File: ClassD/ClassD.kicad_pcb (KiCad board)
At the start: 2 copper layers, 70.2 x 45.3 mm, 39 parts, among them J1 RCJ-01X, J2 RCJ-01X, P1 CONN_01X02, SW1 FSM2JSMAA, U1 AP1117E50G-13, U2 TPA2008D2

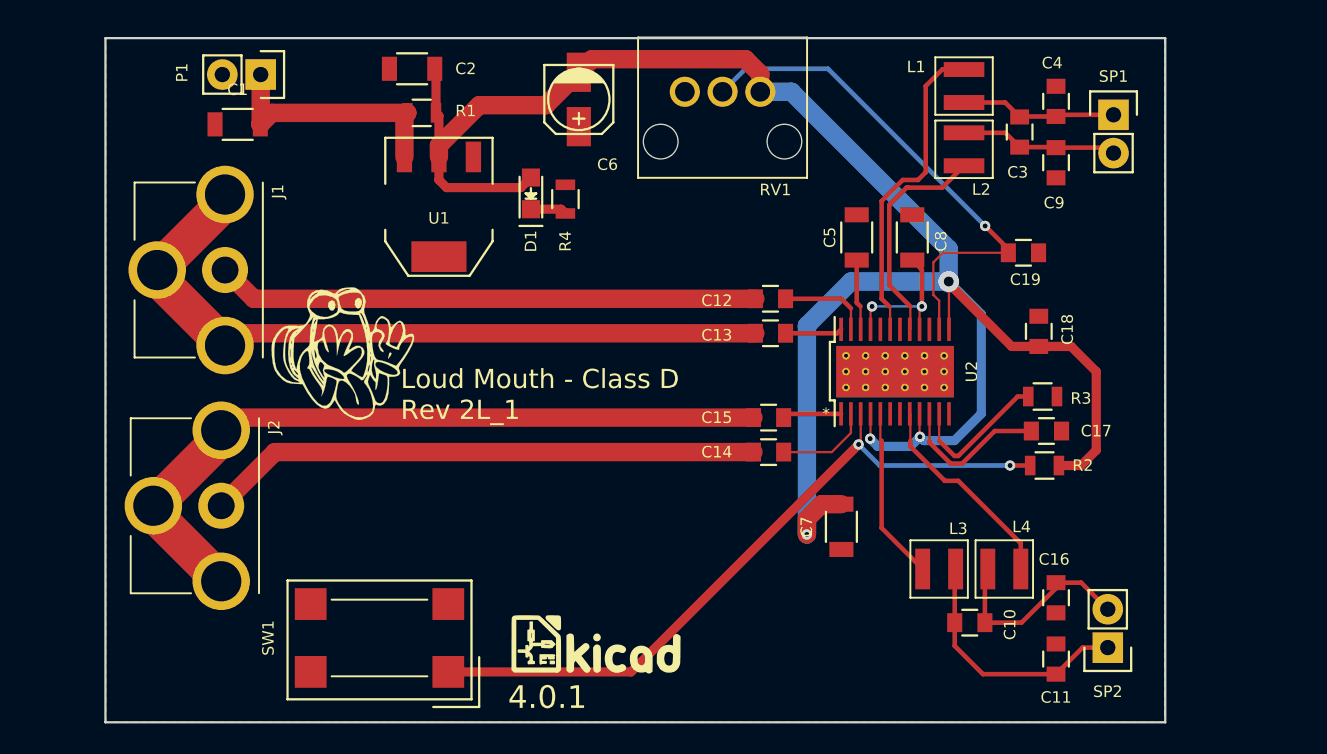
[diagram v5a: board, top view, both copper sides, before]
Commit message: Stitched the ground planes
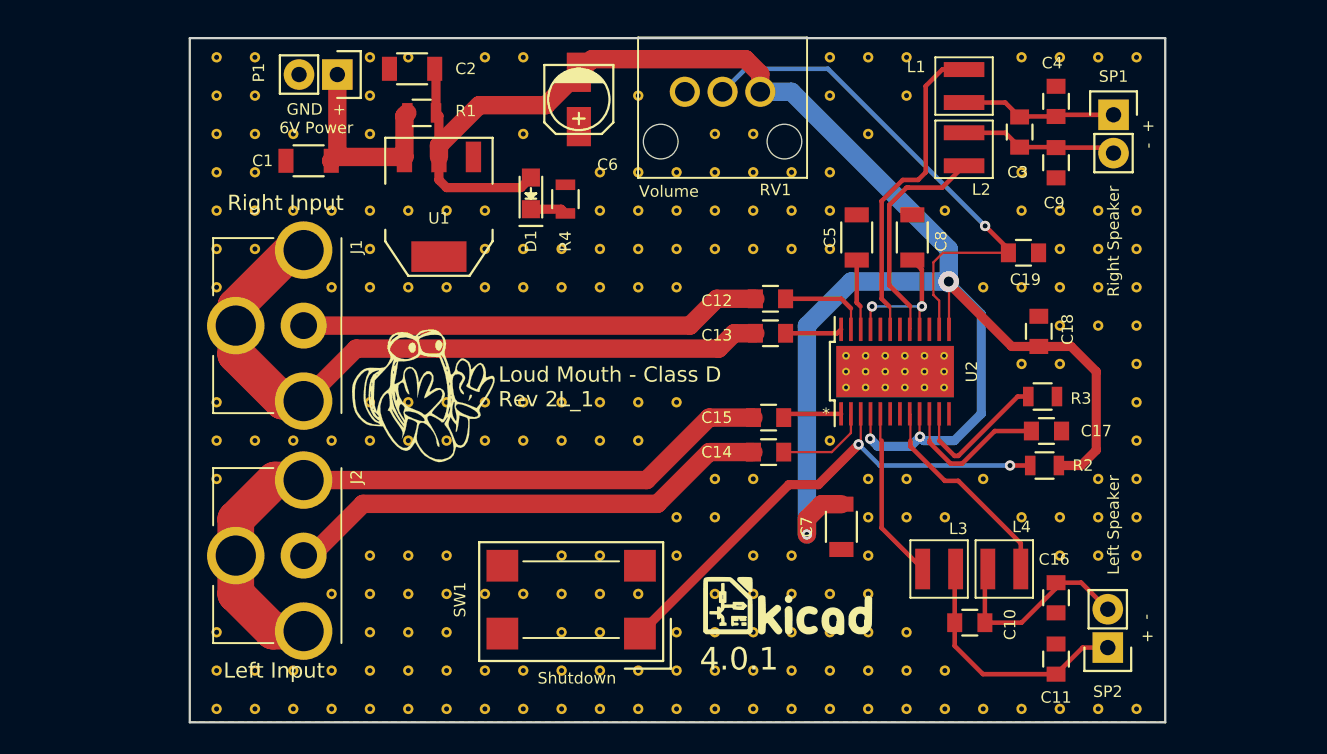
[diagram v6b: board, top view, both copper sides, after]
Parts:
- added ST**111111010: Stitch_VIA, LoudMouth-ClassD:Stitch_VIA, F.Cu at (123.2, 106.7)
- added ST**111111011: Stitch_VIA, LoudMouth-ClassD:Stitch_VIA, F.Cu at (123.2, 109.2)
- added ST**111111014: Stitch_VIA, LoudMouth-ClassD:Stitch_VIA, F.Cu at (123.2, 116.8)
- added ST**111111015: Stitch_VIA, LoudMouth-ClassD:Stitch_VIA, F.Cu at (123.2, 119.4)
- added ST**111111016: Stitch_VIA, LoudMouth-ClassD:Stitch_VIA, F.Cu at (123.2, 121.9)
- added ST**111111017: Stitch_VIA, LoudMouth-ClassD:Stitch_VIA, F.Cu at (123.2, 124.5)
- added ST**111111018: Stitch_VIA, LoudMouth-ClassD:Stitch_VIA, F.Cu at (123.2, 127.0)
- added ST**11111106: Stitch_VIA, LoudMouth-ClassD:Stitch_VIA, F.Cu at (123.2, 96.5)
- added ST**11111107: Stitch_VIA, LoudMouth-ClassD:Stitch_VIA, F.Cu at (123.2, 99.1)
- added ST**1111111: Stitch_VIA, LoudMouth-ClassD:Stitch_VIA, F.Cu at (100.3, 83.8)
- added ST**11111110: Stitch_VIA, LoudMouth-ClassD:Stitch_VIA, F.Cu at (100.3, 106.7)
- added ST**11111111: Stitch_VIA, LoudMouth-ClassD:Stitch_VIA, F.Cu at (100.3, 109.2)
- added ST**111111110: Stitch_VIA, LoudMouth-ClassD:Stitch_VIA, F.Cu at (125.7, 106.7)
- added ST**111111111: Stitch_VIA, LoudMouth-ClassD:Stitch_VIA, F.Cu at (125.7, 109.2)
- added ST**111111114: Stitch_VIA, LoudMouth-ClassD:Stitch_VIA, F.Cu at (125.7, 116.8)
- added ST**111111115: Stitch_VIA, LoudMouth-ClassD:Stitch_VIA, F.Cu at (125.7, 119.4)
- added ST**111111116: Stitch_VIA, LoudMouth-ClassD:Stitch_VIA, F.Cu at (125.7, 121.9)
- added ST**111111117: Stitch_VIA, LoudMouth-ClassD:Stitch_VIA, F.Cu at (125.7, 124.5)
- added ST**111111118: Stitch_VIA, LoudMouth-ClassD:Stitch_VIA, F.Cu at (125.7, 127.0)
- added ST**11111112: Stitch_VIA, LoudMouth-ClassD:Stitch_VIA, F.Cu at (100.3, 111.8)
- added ST**11111114: Stitch_VIA, LoudMouth-ClassD:Stitch_VIA, F.Cu at (125.7, 91.4)
- added ST**11111115: Stitch_VIA, LoudMouth-ClassD:Stitch_VIA, F.Cu at (125.7, 94.0)
- added ST**11111116: Stitch_VIA, LoudMouth-ClassD:Stitch_VIA, F.Cu at (100.3, 121.9)
- added ST**11111116: Stitch_VIA, LoudMouth-ClassD:Stitch_VIA, F.Cu at (125.7, 96.5)
- added ST**11111117: Stitch_VIA, LoudMouth-ClassD:Stitch_VIA, F.Cu at (100.3, 124.5)
- added ST**11111117: Stitch_VIA, LoudMouth-ClassD:Stitch_VIA, F.Cu at (125.7, 99.1)
- added ST**11111118: Stitch_VIA, LoudMouth-ClassD:Stitch_VIA, F.Cu at (100.3, 127.0)
- added ST**1111112: Stitch_VIA, LoudMouth-ClassD:Stitch_VIA, F.Cu at (100.3, 86.4)
- added ST**111111210: Stitch_VIA, LoudMouth-ClassD:Stitch_VIA, F.Cu at (128.3, 106.7)
- added ST**111111211: Stitch_VIA, LoudMouth-ClassD:Stitch_VIA, F.Cu at (128.3, 109.2)
- added ST**111111215: Stitch_VIA, LoudMouth-ClassD:Stitch_VIA, F.Cu at (128.3, 119.4)
- added ST**111111217: Stitch_VIA, LoudMouth-ClassD:Stitch_VIA, F.Cu at (128.3, 124.5)
- added ST**111111218: Stitch_VIA, LoudMouth-ClassD:Stitch_VIA, F.Cu at (128.3, 127.0)
- added ST**11111122: Stitch_VIA, LoudMouth-ClassD:Stitch_VIA, F.Cu at (128.3, 86.4)
- added ST**11111124: Stitch_VIA, LoudMouth-ClassD:Stitch_VIA, F.Cu at (128.3, 91.4)
- added ST**11111125: Stitch_VIA, LoudMouth-ClassD:Stitch_VIA, F.Cu at (128.3, 94.0)
- added ST**11111126: Stitch_VIA, LoudMouth-ClassD:Stitch_VIA, F.Cu at (128.3, 96.5)
- added ST**11111127: Stitch_VIA, LoudMouth-ClassD:Stitch_VIA, F.Cu at (128.3, 99.1)
- added ST**1111113: Stitch_VIA, LoudMouth-ClassD:Stitch_VIA, F.Cu at (100.3, 88.9)
- added ST**111111310: Stitch_VIA, LoudMouth-ClassD:Stitch_VIA, F.Cu at (130.8, 106.7)
- added ST**111111313: Stitch_VIA, LoudMouth-ClassD:Stitch_VIA, F.Cu at (130.8, 114.3)
- added ST**111111314: Stitch_VIA, LoudMouth-ClassD:Stitch_VIA, F.Cu at (130.8, 116.8)
- added ST**111111316: Stitch_VIA, LoudMouth-ClassD:Stitch_VIA, F.Cu at (130.8, 121.9)
- added ST**111111317: Stitch_VIA, LoudMouth-ClassD:Stitch_VIA, F.Cu at (130.8, 124.5)
- added ST**111111318: Stitch_VIA, LoudMouth-ClassD:Stitch_VIA, F.Cu at (130.8, 127.0)
- added ST**11111134: Stitch_VIA, LoudMouth-ClassD:Stitch_VIA, F.Cu at (130.8, 91.4)
- added ST**11111135: Stitch_VIA, LoudMouth-ClassD:Stitch_VIA, F.Cu at (130.8, 94.0)
- added ST**11111136: Stitch_VIA, LoudMouth-ClassD:Stitch_VIA, F.Cu at (130.8, 96.5)
- added ST**11111137: Stitch_VIA, LoudMouth-ClassD:Stitch_VIA, F.Cu at (130.8, 99.1)
- added ST**1111114: Stitch_VIA, LoudMouth-ClassD:Stitch_VIA, F.Cu at (100.3, 91.4)
- added ST**111111412: Stitch_VIA, LoudMouth-ClassD:Stitch_VIA, F.Cu at (133.3, 111.8)
- added ST**111111413: Stitch_VIA, LoudMouth-ClassD:Stitch_VIA, F.Cu at (133.3, 114.3)
- added ST**111111415: Stitch_VIA, LoudMouth-ClassD:Stitch_VIA, F.Cu at (133.3, 119.4)
- added ST**111111416: Stitch_VIA, LoudMouth-ClassD:Stitch_VIA, F.Cu at (133.3, 121.9)
- added ST**111111417: Stitch_VIA, LoudMouth-ClassD:Stitch_VIA, F.Cu at (133.3, 124.5)
- added ST**111111418: Stitch_VIA, LoudMouth-ClassD:Stitch_VIA, F.Cu at (133.3, 127.0)
- added ST**11111143: Stitch_VIA, LoudMouth-ClassD:Stitch_VIA, F.Cu at (133.3, 88.9)
- added ST**11111144: Stitch_VIA, LoudMouth-ClassD:Stitch_VIA, F.Cu at (133.3, 91.4)
- added ST**11111145: Stitch_VIA, LoudMouth-ClassD:Stitch_VIA, F.Cu at (133.3, 94.0)
- added ST**11111146: Stitch_VIA, LoudMouth-ClassD:Stitch_VIA, F.Cu at (133.3, 96.5)
- added ST**1111115: Stitch_VIA, LoudMouth-ClassD:Stitch_VIA, F.Cu at (100.3, 94.0)
- added ST**111111512: Stitch_VIA, LoudMouth-ClassD:Stitch_VIA, F.Cu at (135.9, 111.8)
- added ST**111111514: Stitch_VIA, LoudMouth-ClassD:Stitch_VIA, F.Cu at (135.9, 116.8)
- added ST**111111515: Stitch_VIA, LoudMouth-ClassD:Stitch_VIA, F.Cu at (135.9, 119.4)
- added ST**111111516: Stitch_VIA, LoudMouth-ClassD:Stitch_VIA, F.Cu at (135.9, 121.9)
- added ST**111111517: Stitch_VIA, LoudMouth-ClassD:Stitch_VIA, F.Cu at (135.9, 124.5)
- added ST**111111518: Stitch_VIA, LoudMouth-ClassD:Stitch_VIA, F.Cu at (135.9, 127.0)
- added ST**11111153: Stitch_VIA, LoudMouth-ClassD:Stitch_VIA, F.Cu at (135.9, 88.9)
- added ST**11111154: Stitch_VIA, LoudMouth-ClassD:Stitch_VIA, F.Cu at (135.9, 91.4)
- added ST**11111155: Stitch_VIA, LoudMouth-ClassD:Stitch_VIA, F.Cu at (135.9, 94.0)
- added ST**11111156: Stitch_VIA, LoudMouth-ClassD:Stitch_VIA, F.Cu at (135.9, 96.5)
- added ST**1111116: Stitch_VIA, LoudMouth-ClassD:Stitch_VIA, F.Cu at (100.3, 96.5)
- added ST**111111614: Stitch_VIA, LoudMouth-ClassD:Stitch_VIA, F.Cu at (138.4, 116.8)
- added ST**111111615: Stitch_VIA, LoudMouth-ClassD:Stitch_VIA, F.Cu at (138.4, 119.4)
- added ST**111111616: Stitch_VIA, LoudMouth-ClassD:Stitch_VIA, F.Cu at (138.4, 121.9)
- added ST**111111617: Stitch_VIA, LoudMouth-ClassD:Stitch_VIA, F.Cu at (138.4, 124.5)
- added ST**111111618: Stitch_VIA, LoudMouth-ClassD:Stitch_VIA, F.Cu at (138.4, 127.0)
- added ST**11111164: Stitch_VIA, LoudMouth-ClassD:Stitch_VIA, F.Cu at (138.4, 91.4)
- added ST**11111165: Stitch_VIA, LoudMouth-ClassD:Stitch_VIA, F.Cu at (138.4, 94.0)
- added ST**11111166: Stitch_VIA, LoudMouth-ClassD:Stitch_VIA, F.Cu at (138.4, 96.5)
- added ST**1111117: Stitch_VIA, LoudMouth-ClassD:Stitch_VIA, F.Cu at (100.3, 99.1)
- added ST**11111171: Stitch_VIA, LoudMouth-ClassD:Stitch_VIA, F.Cu at (141.0, 83.8)
- added ST**111111711: Stitch_VIA, LoudMouth-ClassD:Stitch_VIA, F.Cu at (141.0, 109.2)
- added ST**111111715: Stitch_VIA, LoudMouth-ClassD:Stitch_VIA, F.Cu at (141.0, 119.4)
- added ST**111111716: Stitch_VIA, LoudMouth-ClassD:Stitch_VIA, F.Cu at (141.0, 121.9)
- added ST**111111717: Stitch_VIA, LoudMouth-ClassD:Stitch_VIA, F.Cu at (141.0, 124.5)
- added ST**111111718: Stitch_VIA, LoudMouth-ClassD:Stitch_VIA, F.Cu at (141.0, 127.0)
- added ST**11111172: Stitch_VIA, LoudMouth-ClassD:Stitch_VIA, F.Cu at (141.0, 86.4)
- added ST**11111174: Stitch_VIA, LoudMouth-ClassD:Stitch_VIA, F.Cu at (141.0, 91.4)
- added ST**11111175: Stitch_VIA, LoudMouth-ClassD:Stitch_VIA, F.Cu at (141.0, 94.0)
- added ST**11111176: Stitch_VIA, LoudMouth-ClassD:Stitch_VIA, F.Cu at (141.0, 96.5)
- added ST**11111181: Stitch_VIA, LoudMouth-ClassD:Stitch_VIA, F.Cu at (143.5, 83.8)
- added ST**111111812: Stitch_VIA, LoudMouth-ClassD:Stitch_VIA, F.Cu at (143.5, 111.8)
- added ST**111111813: Stitch_VIA, LoudMouth-ClassD:Stitch_VIA, F.Cu at (143.5, 114.3)
- added ST**111111814: Stitch_VIA, LoudMouth-ClassD:Stitch_VIA, F.Cu at (143.5, 116.8)
- added ST**111111815: Stitch_VIA, LoudMouth-ClassD:Stitch_VIA, F.Cu at (143.5, 119.4)
- added ST**111111816: Stitch_VIA, LoudMouth-ClassD:Stitch_VIA, F.Cu at (143.5, 121.9)
- added ST**111111817: Stitch_VIA, LoudMouth-ClassD:Stitch_VIA, F.Cu at (143.5, 124.5)
- added ST**111111818: Stitch_VIA, LoudMouth-ClassD:Stitch_VIA, F.Cu at (143.5, 127.0)
- added ST**11111183: Stitch_VIA, LoudMouth-ClassD:Stitch_VIA, F.Cu at (143.5, 88.9)
- added ST**11111191: Stitch_VIA, LoudMouth-ClassD:Stitch_VIA, F.Cu at (146.1, 83.8)
- added ST**111111912: Stitch_VIA, LoudMouth-ClassD:Stitch_VIA, F.Cu at (146.1, 111.8)
- added ST**111111913: Stitch_VIA, LoudMouth-ClassD:Stitch_VIA, F.Cu at (146.1, 114.3)
- added ST**111111916: Stitch_VIA, LoudMouth-ClassD:Stitch_VIA, F.Cu at (146.1, 121.9)
- added ST**111111917: Stitch_VIA, LoudMouth-ClassD:Stitch_VIA, F.Cu at (146.1, 124.5)
- added ST**111111918: Stitch_VIA, LoudMouth-ClassD:Stitch_VIA, F.Cu at (146.1, 127.0)
- added ST**11111192: Stitch_VIA, LoudMouth-ClassD:Stitch_VIA, F.Cu at (146.1, 86.4)
- added ST**111112013: Stitch_VIA, LoudMouth-ClassD:Stitch_VIA, F.Cu at (148.6, 114.3)
- added ST**111112017: Stitch_VIA, LoudMouth-ClassD:Stitch_VIA, F.Cu at (148.6, 124.5)
- added ST**111112018: Stitch_VIA, LoudMouth-ClassD:Stitch_VIA, F.Cu at (148.6, 127.0)
- added ST**11111205: Stitch_VIA, LoudMouth-ClassD:Stitch_VIA, F.Cu at (148.6, 94.0)
- added ST**1111121: Stitch_VIA, LoudMouth-ClassD:Stitch_VIA, F.Cu at (102.9, 83.8)
- added ST**11111211: Stitch_VIA, LoudMouth-ClassD:Stitch_VIA, F.Cu at (102.9, 109.2)
- added ST**111112112: Stitch_VIA, LoudMouth-ClassD:Stitch_VIA, F.Cu at (151.1, 111.8)
- added ST**111112118: Stitch_VIA, LoudMouth-ClassD:Stitch_VIA, F.Cu at (151.1, 127.0)
- added ST**11111217: Stitch_VIA, LoudMouth-ClassD:Stitch_VIA, F.Cu at (102.9, 124.5)
- added ST**11111217: Stitch_VIA, LoudMouth-ClassD:Stitch_VIA, F.Cu at (151.1, 99.1)
- added ST**11111218: Stitch_VIA, LoudMouth-ClassD:Stitch_VIA, F.Cu at (102.9, 127.0)
- added ST**1111122: Stitch_VIA, LoudMouth-ClassD:Stitch_VIA, F.Cu at (102.9, 86.4)
- added ST**11111221: Stitch_VIA, LoudMouth-ClassD:Stitch_VIA, F.Cu at (153.7, 83.8)
- added ST**111112213: Stitch_VIA, LoudMouth-ClassD:Stitch_VIA, F.Cu at (153.7, 114.3)
- added ST**111112218: Stitch_VIA, LoudMouth-ClassD:Stitch_VIA, F.Cu at (153.7, 127.0)
- added ST**11111224: Stitch_VIA, LoudMouth-ClassD:Stitch_VIA, F.Cu at (153.7, 91.4)
- added ST**11111225: Stitch_VIA, LoudMouth-ClassD:Stitch_VIA, F.Cu at (153.7, 94.0)
- added ST**11111227: Stitch_VIA, LoudMouth-ClassD:Stitch_VIA, F.Cu at (153.7, 99.1)
- added ST**11111229: Stitch_VIA, LoudMouth-ClassD:Stitch_VIA, F.Cu at (153.7, 104.1)
- added ST**1111123: Stitch_VIA, LoudMouth-ClassD:Stitch_VIA, F.Cu at (102.9, 88.9)
- added ST**11111231: Stitch_VIA, LoudMouth-ClassD:Stitch_VIA, F.Cu at (156.2, 83.8)
- added ST**111112313: Stitch_VIA, LoudMouth-ClassD:Stitch_VIA, F.Cu at (156.2, 114.3)
- added ST**111112314: Stitch_VIA, LoudMouth-ClassD:Stitch_VIA, F.Cu at (156.2, 116.8)
- added ST**111112318: Stitch_VIA, LoudMouth-ClassD:Stitch_VIA, F.Cu at (156.2, 127.0)
- added ST**11111235: Stitch_VIA, LoudMouth-ClassD:Stitch_VIA, F.Cu at (156.2, 94.0)
- added ST**11111236: Stitch_VIA, LoudMouth-ClassD:Stitch_VIA, F.Cu at (156.2, 96.5)
- added ST**11111237: Stitch_VIA, LoudMouth-ClassD:Stitch_VIA, F.Cu at (156.2, 99.1)
- added ST**11111238: Stitch_VIA, LoudMouth-ClassD:Stitch_VIA, F.Cu at (156.2, 101.6)
- added ST**11111239: Stitch_VIA, LoudMouth-ClassD:Stitch_VIA, F.Cu at (156.2, 104.1)
- added ST**1111124: Stitch_VIA, LoudMouth-ClassD:Stitch_VIA, F.Cu at (102.9, 91.4)
- added ST**11111241: Stitch_VIA, LoudMouth-ClassD:Stitch_VIA, F.Cu at (158.8, 83.8)
- added ST**111112412: Stitch_VIA, LoudMouth-ClassD:Stitch_VIA, F.Cu at (158.8, 111.8)
- added ST**111112413: Stitch_VIA, LoudMouth-ClassD:Stitch_VIA, F.Cu at (158.8, 114.3)
- added ST**111112414: Stitch_VIA, LoudMouth-ClassD:Stitch_VIA, F.Cu at (158.8, 116.8)
- added ST**111112418: Stitch_VIA, LoudMouth-ClassD:Stitch_VIA, F.Cu at (158.8, 127.0)
- added ST**11111245: Stitch_VIA, LoudMouth-ClassD:Stitch_VIA, F.Cu at (158.8, 94.0)
- added ST**11111246: Stitch_VIA, LoudMouth-ClassD:Stitch_VIA, F.Cu at (158.8, 96.5)
- added ST**11111247: Stitch_VIA, LoudMouth-ClassD:Stitch_VIA, F.Cu at (158.8, 99.1)
- added ST**11111248: Stitch_VIA, LoudMouth-ClassD:Stitch_VIA, F.Cu at (158.8, 101.6)
- added ST**1111125: Stitch_VIA, LoudMouth-ClassD:Stitch_VIA, F.Cu at (102.9, 94.0)
- added ST**11111251: Stitch_VIA, LoudMouth-ClassD:Stitch_VIA, F.Cu at (161.3, 83.8)
- added ST**111112510: Stitch_VIA, LoudMouth-ClassD:Stitch_VIA, F.Cu at (161.3, 106.7)
- added ST**111112511: Stitch_VIA, LoudMouth-ClassD:Stitch_VIA, F.Cu at (161.3, 109.2)
- added ST**111112512: Stitch_VIA, LoudMouth-ClassD:Stitch_VIA, F.Cu at (161.3, 111.8)
- added ST**111112513: Stitch_VIA, LoudMouth-ClassD:Stitch_VIA, F.Cu at (161.3, 114.3)
- added ST**111112514: Stitch_VIA, LoudMouth-ClassD:Stitch_VIA, F.Cu at (161.3, 116.8)
- added ST**111112518: Stitch_VIA, LoudMouth-ClassD:Stitch_VIA, F.Cu at (161.3, 127.0)
- added ST**11111255: Stitch_VIA, LoudMouth-ClassD:Stitch_VIA, F.Cu at (161.3, 94.0)
- added ST**11111256: Stitch_VIA, LoudMouth-ClassD:Stitch_VIA, F.Cu at (161.3, 96.5)
- added ST**11111257: Stitch_VIA, LoudMouth-ClassD:Stitch_VIA, F.Cu at (161.3, 99.1)
- added ST**11111258: Stitch_VIA, LoudMouth-ClassD:Stitch_VIA, F.Cu at (161.3, 101.6)
- added ST**11111259: Stitch_VIA, LoudMouth-ClassD:Stitch_VIA, F.Cu at (161.3, 104.1)
- added ST**1111126: Stitch_VIA, LoudMouth-ClassD:Stitch_VIA, F.Cu at (102.9, 96.5)
- added ST**11111311: Stitch_VIA, LoudMouth-ClassD:Stitch_VIA, F.Cu at (105.4, 109.2)
- added ST**11111317: Stitch_VIA, LoudMouth-ClassD:Stitch_VIA, F.Cu at (105.4, 124.5)
- added ST**11111318: Stitch_VIA, LoudMouth-ClassD:Stitch_VIA, F.Cu at (105.4, 127.0)
- added ST**1111134: Stitch_VIA, LoudMouth-ClassD:Stitch_VIA, F.Cu at (105.4, 88.9)
- added ST**1111135: Stitch_VIA, LoudMouth-ClassD:Stitch_VIA, F.Cu at (105.4, 94.0)
- added ST**11111411: Stitch_VIA, LoudMouth-ClassD:Stitch_VIA, F.Cu at (108.0, 109.2)
- added ST**11111415: Stitch_VIA, LoudMouth-ClassD:Stitch_VIA, F.Cu at (108.0, 119.4)
- added ST**11111417: Stitch_VIA, LoudMouth-ClassD:Stitch_VIA, F.Cu at (108.0, 124.5)
- added ST**11111418: Stitch_VIA, LoudMouth-ClassD:Stitch_VIA, F.Cu at (108.0, 127.0)
- added ST**1111145: Stitch_VIA, LoudMouth-ClassD:Stitch_VIA, F.Cu at (108.0, 94.0)
- added ST**1111147: Stitch_VIA, LoudMouth-ClassD:Stitch_VIA, F.Cu at (108.0, 99.1)
- added ST**1111151: Stitch_VIA, LoudMouth-ClassD:Stitch_VIA, F.Cu at (110.5, 83.8)
- added ST**11111510: Stitch_VIA, LoudMouth-ClassD:Stitch_VIA, F.Cu at (110.5, 106.7)
- added ST**11111511: Stitch_VIA, LoudMouth-ClassD:Stitch_VIA, F.Cu at (110.5, 109.2)
- added ST**11111514: Stitch_VIA, LoudMouth-ClassD:Stitch_VIA, F.Cu at (110.5, 116.8)
- added ST**11111515: Stitch_VIA, LoudMouth-ClassD:Stitch_VIA, F.Cu at (110.5, 119.4)
- added ST**11111516: Stitch_VIA, LoudMouth-ClassD:Stitch_VIA, F.Cu at (110.5, 121.9)
- added ST**11111517: Stitch_VIA, LoudMouth-ClassD:Stitch_VIA, F.Cu at (110.5, 124.5)
- added ST**11111518: Stitch_VIA, LoudMouth-ClassD:Stitch_VIA, F.Cu at (110.5, 127.0)
- added ST**1111152: Stitch_VIA, LoudMouth-ClassD:Stitch_VIA, F.Cu at (110.5, 86.4)
- added ST**1111153: Stitch_VIA, LoudMouth-ClassD:Stitch_VIA, F.Cu at (110.5, 88.9)
- added ST**1111155: Stitch_VIA, LoudMouth-ClassD:Stitch_VIA, F.Cu at (110.5, 94.0)
- added ST**1111156: Stitch_VIA, LoudMouth-ClassD:Stitch_VIA, F.Cu at (110.5, 96.5)
- added ST**1111157: Stitch_VIA, LoudMouth-ClassD:Stitch_VIA, F.Cu at (110.5, 99.1)
- added ST**1111161: Stitch_VIA, LoudMouth-ClassD:Stitch_VIA, F.Cu at (113.0, 83.8)
- added ST**11111610: Stitch_VIA, LoudMouth-ClassD:Stitch_VIA, F.Cu at (113.0, 106.7)
- added ST**11111611: Stitch_VIA, LoudMouth-ClassD:Stitch_VIA, F.Cu at (113.0, 109.2)
- added ST**11111614: Stitch_VIA, LoudMouth-ClassD:Stitch_VIA, F.Cu at (113.0, 116.8)
- added ST**11111615: Stitch_VIA, LoudMouth-ClassD:Stitch_VIA, F.Cu at (113.0, 119.4)
- added ST**11111616: Stitch_VIA, LoudMouth-ClassD:Stitch_VIA, F.Cu at (113.0, 121.9)
- added ST**11111617: Stitch_VIA, LoudMouth-ClassD:Stitch_VIA, F.Cu at (113.0, 124.5)
- added ST**11111618: Stitch_VIA, LoudMouth-ClassD:Stitch_VIA, F.Cu at (113.0, 127.0)
- added ST**1111165: Stitch_VIA, LoudMouth-ClassD:Stitch_VIA, F.Cu at (113.0, 94.0)
- added ST**1111167: Stitch_VIA, LoudMouth-ClassD:Stitch_VIA, F.Cu at (113.0, 99.1)
- added ST**11111710: Stitch_VIA, LoudMouth-ClassD:Stitch_VIA, F.Cu at (115.6, 106.7)
- added ST**11111711: Stitch_VIA, LoudMouth-ClassD:Stitch_VIA, F.Cu at (115.6, 109.2)
- added ST**11111714: Stitch_VIA, LoudMouth-ClassD:Stitch_VIA, F.Cu at (115.6, 116.8)
- added ST**11111715: Stitch_VIA, LoudMouth-ClassD:Stitch_VIA, F.Cu at (115.6, 119.4)
- added ST**11111716: Stitch_VIA, LoudMouth-ClassD:Stitch_VIA, F.Cu at (115.6, 121.9)
- added ST**11111717: Stitch_VIA, LoudMouth-ClassD:Stitch_VIA, F.Cu at (115.6, 124.5)
- added ST**11111718: Stitch_VIA, LoudMouth-ClassD:Stitch_VIA, F.Cu at (115.6, 127.0)
- added ST**1111175: Stitch_VIA, LoudMouth-ClassD:Stitch_VIA, F.Cu at (115.6, 94.0)
- added ST**1111177: Stitch_VIA, LoudMouth-ClassD:Stitch_VIA, F.Cu at (115.6, 99.1)
- added ST**1111181: Stitch_VIA, LoudMouth-ClassD:Stitch_VIA, F.Cu at (118.1, 83.8)
- added ST**11111810: Stitch_VIA, LoudMouth-ClassD:Stitch_VIA, F.Cu at (118.1, 106.7)
- added ST**11111811: Stitch_VIA, LoudMouth-ClassD:Stitch_VIA, F.Cu at (118.1, 109.2)
- added ST**11111815: Stitch_VIA, LoudMouth-ClassD:Stitch_VIA, F.Cu at (118.1, 119.4)
- added ST**11111817: Stitch_VIA, LoudMouth-ClassD:Stitch_VIA, F.Cu at (118.1, 124.5)
- added ST**11111818: Stitch_VIA, LoudMouth-ClassD:Stitch_VIA, F.Cu at (118.1, 127.0)
- added ST**1111185: Stitch_VIA, LoudMouth-ClassD:Stitch_VIA, F.Cu at (118.1, 94.0)
- added ST**1111186: Stitch_VIA, LoudMouth-ClassD:Stitch_VIA, F.Cu at (118.1, 96.5)
- added ST**1111187: Stitch_VIA, LoudMouth-ClassD:Stitch_VIA, F.Cu at (118.1, 99.1)
- added ST**1111191: Stitch_VIA, LoudMouth-ClassD:Stitch_VIA, F.Cu at (120.7, 83.8)
- added ST**11111910: Stitch_VIA, LoudMouth-ClassD:Stitch_VIA, F.Cu at (120.7, 106.7)
- added ST**11111911: Stitch_VIA, LoudMouth-ClassD:Stitch_VIA, F.Cu at (120.7, 109.2)
- added ST**11111915: Stitch_VIA, LoudMouth-ClassD:Stitch_VIA, F.Cu at (120.7, 119.4)
- added ST**11111917: Stitch_VIA, LoudMouth-ClassD:Stitch_VIA, F.Cu at (120.7, 124.5)
- added ST**11111918: Stitch_VIA, LoudMouth-ClassD:Stitch_VIA, F.Cu at (120.7, 127.0)
- added ST**1111193: Stitch_VIA, LoudMouth-ClassD:Stitch_VIA, F.Cu at (120.7, 88.9)
- added ST**1111196: Stitch_VIA, LoudMouth-ClassD:Stitch_VIA, F.Cu at (120.7, 96.5)
- added ST**1111197: Stitch_VIA, LoudMouth-ClassD:Stitch_VIA, F.Cu at (120.7, 99.1)
- moved SW1 13.0 mm to (123.8, 119.8)
- moved LOGO2 13.0 mm to (138.2, 120.1)
- moved J2 6.38 mm to (101.6, 116.8)
- moved J1 6.38 mm to (101.6, 101.6)
- moved LOGO1 6.02 mm to (114.0, 106.2)
- moved C1 5.28 mm to (106.4, 90.7)
- moved P1 5.08 mm to (108.3, 85.0)
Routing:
- net /~SHUTDOWN: track 47.5 -> 33.7 mm
- net /RIN+: track 35.9 -> 30.7 mm
- net /LIN+: track 36.7 -> 32.7 mm
- net /VIN: track 16.4 -> 13.8 mm
- net /RIN-: track 49.2 -> 46.8 mm
- net /LIN-: track 49.4 -> 47.6 mm
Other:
- board size 70.2 x 45.3 mm -> 64.6 x 45.3 mm
- board text added: "- +"
- board text added: "GND + 6V Power"
- board text added: "Left Input"
- board text added: "Left Speaker"
- board text added: "Right Input"
- board text added: "Right Speaker"
- board text added: "Shutdown"
- board text added: "Volume"

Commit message: Updated the layout with some circuit changes as well as the audio chip footprint.
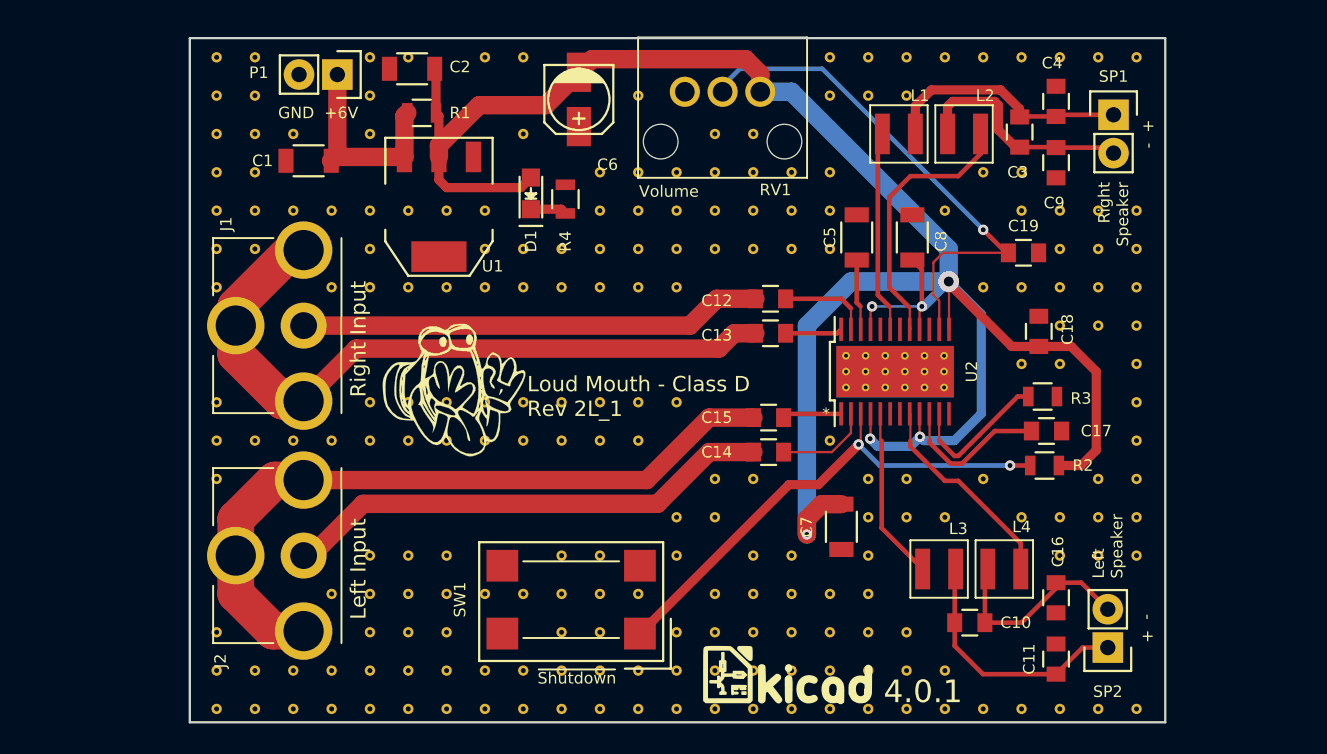
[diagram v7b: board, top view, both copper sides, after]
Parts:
- removed ST**11111183, ST**11111191, ST**11111192: Stitch_VIA, LoudMouth-ClassD:Stitch_VIA
- added ST**111111812: Stitch_VIA, LoudMouth-ClassD:Stitch_VIA, F.Cu at (143.5, 86.4)
- added ST**1111118211: Stitch_VIA, LoudMouth-ClassD:Stitch_VIA, F.Cu at (146.1, 83.8)
- added ST**111111822: Stitch_VIA, LoudMouth-ClassD:Stitch_VIA, F.Cu at (146.1, 86.4)
- added ST**1111118221: Stitch_VIA, LoudMouth-ClassD:Stitch_VIA, F.Cu at (148.6, 83.8)
- added ST**1111118231: Stitch_VIA, LoudMouth-ClassD:Stitch_VIA, F.Cu at (151.1, 83.8)
- added ST**11111225: Stitch_VIA, LoudMouth-ClassD:Stitch_VIA, F.Cu at (151.1, 91.4)
- moved L1 5.36 mm to (145.5, 88.9), turned to 90 degrees
- moved LOGO2 4.57 mm to (138.2, 124.7)
- moved LOGO1 2.07 mm to (116.1, 105.8)
- moved L2 1.02 mm to (149.9, 88.9), turned to 270 degrees
- renumbered ST**11111181 to ST**111111811
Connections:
- net Net-(C5-Pad2) renamed /BYPASS
- net Net-(L1-Pad1) renamed /ROUTP
- net Net-(L2-Pad1) renamed /ROUTN
- net Net-(L4-Pad1) renamed /LOUTN
- C8 pad 2: Net-(C8-Pad2) -> /VDD
- U2 pad 16: Net-(C8-Pad2) -> /VDD
- U2 pad 21: Net-(C8-Pad2) -> /VDD
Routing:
- net /VDD: track 132.7 -> 145.3 mm, vias 4 -> 6
- net Net-(C8-Pad2): track 10.2 -> 0.00 mm, vias 2 -> 0
- net /ROUTP: track 21.2 -> 13.4 mm
- net /ROUT+: track 10.4 -> 16.5 mm
- net /ROUT-: track 10.5 -> 15.4 mm
- net /ROUTN: track 14.9 -> 18.0 mm
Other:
- board text added: "GND +6V"
- board text added: "~Shutdown"
- board text removed: "GND + 6V Power"
- board text removed: "Shutdown"
